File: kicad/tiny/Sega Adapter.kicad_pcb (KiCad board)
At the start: 2 copper layers, 25.4 x 25.4 mm, 5 parts, among them U1 PIC16F1847

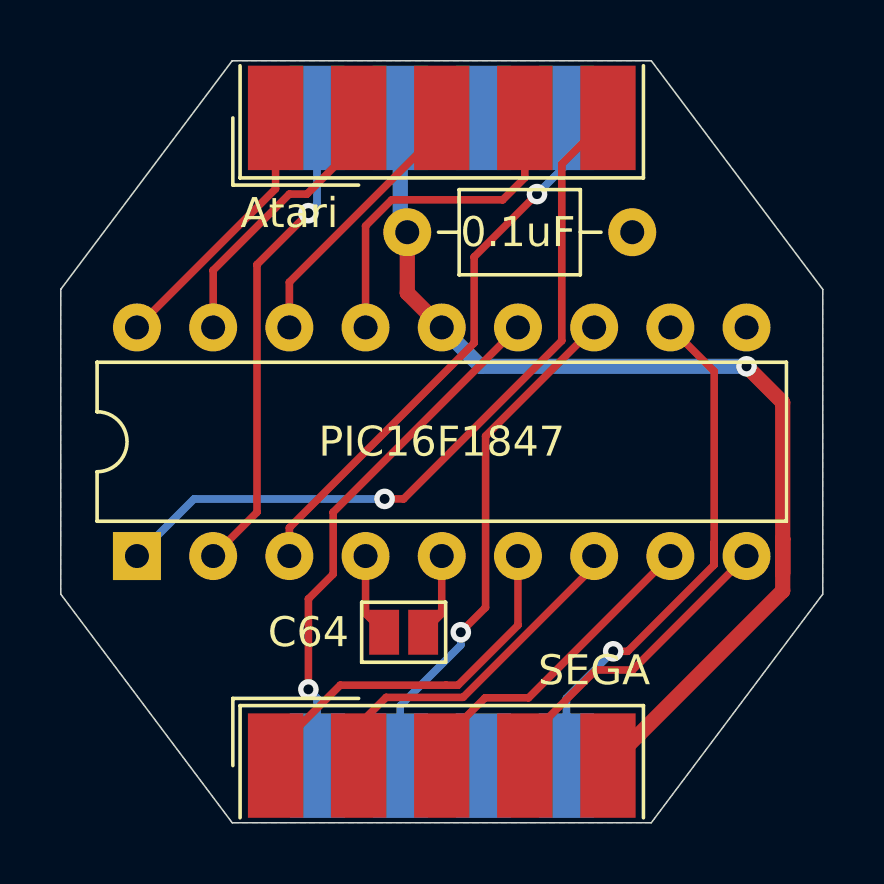
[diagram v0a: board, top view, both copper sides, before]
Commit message: Add README and licence
Also tweak the PCBs:
- round the corners of the full PCB
- add a copyright message to the full and tiny PCBs
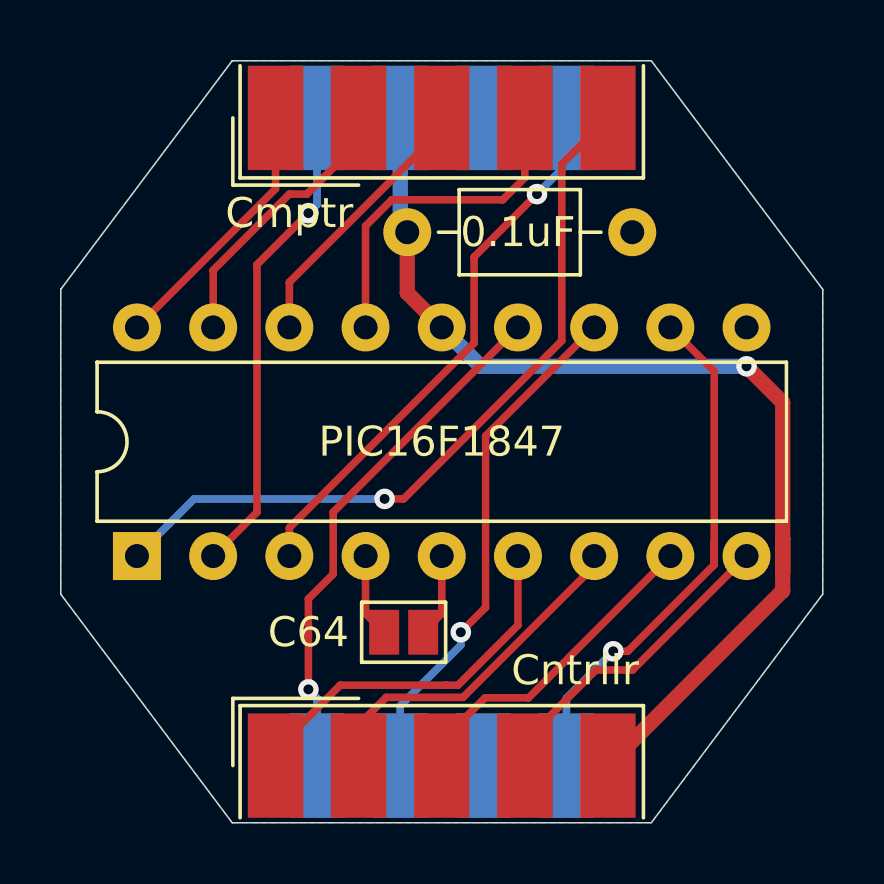
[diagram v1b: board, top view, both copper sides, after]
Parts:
- renumbered Atari to Cmptr, SEGA to Cntrllr
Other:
- board text added: "Sega Controller Adapter © 2021 Eyvind Bernhardsen"
